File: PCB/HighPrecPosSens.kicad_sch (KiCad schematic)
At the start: 85 parts, among them J1 Conn_01x02_Male, J2 Conn_01x02_Male, J3 Conn_01x02_Male, J4 Conn_01x02_Male, J5 Conn_01x06_Male, U1 ST1S14PHR, U2 S12443, U3 LM393DR2G, U4 LM393DR2G, U5 74LVC541A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

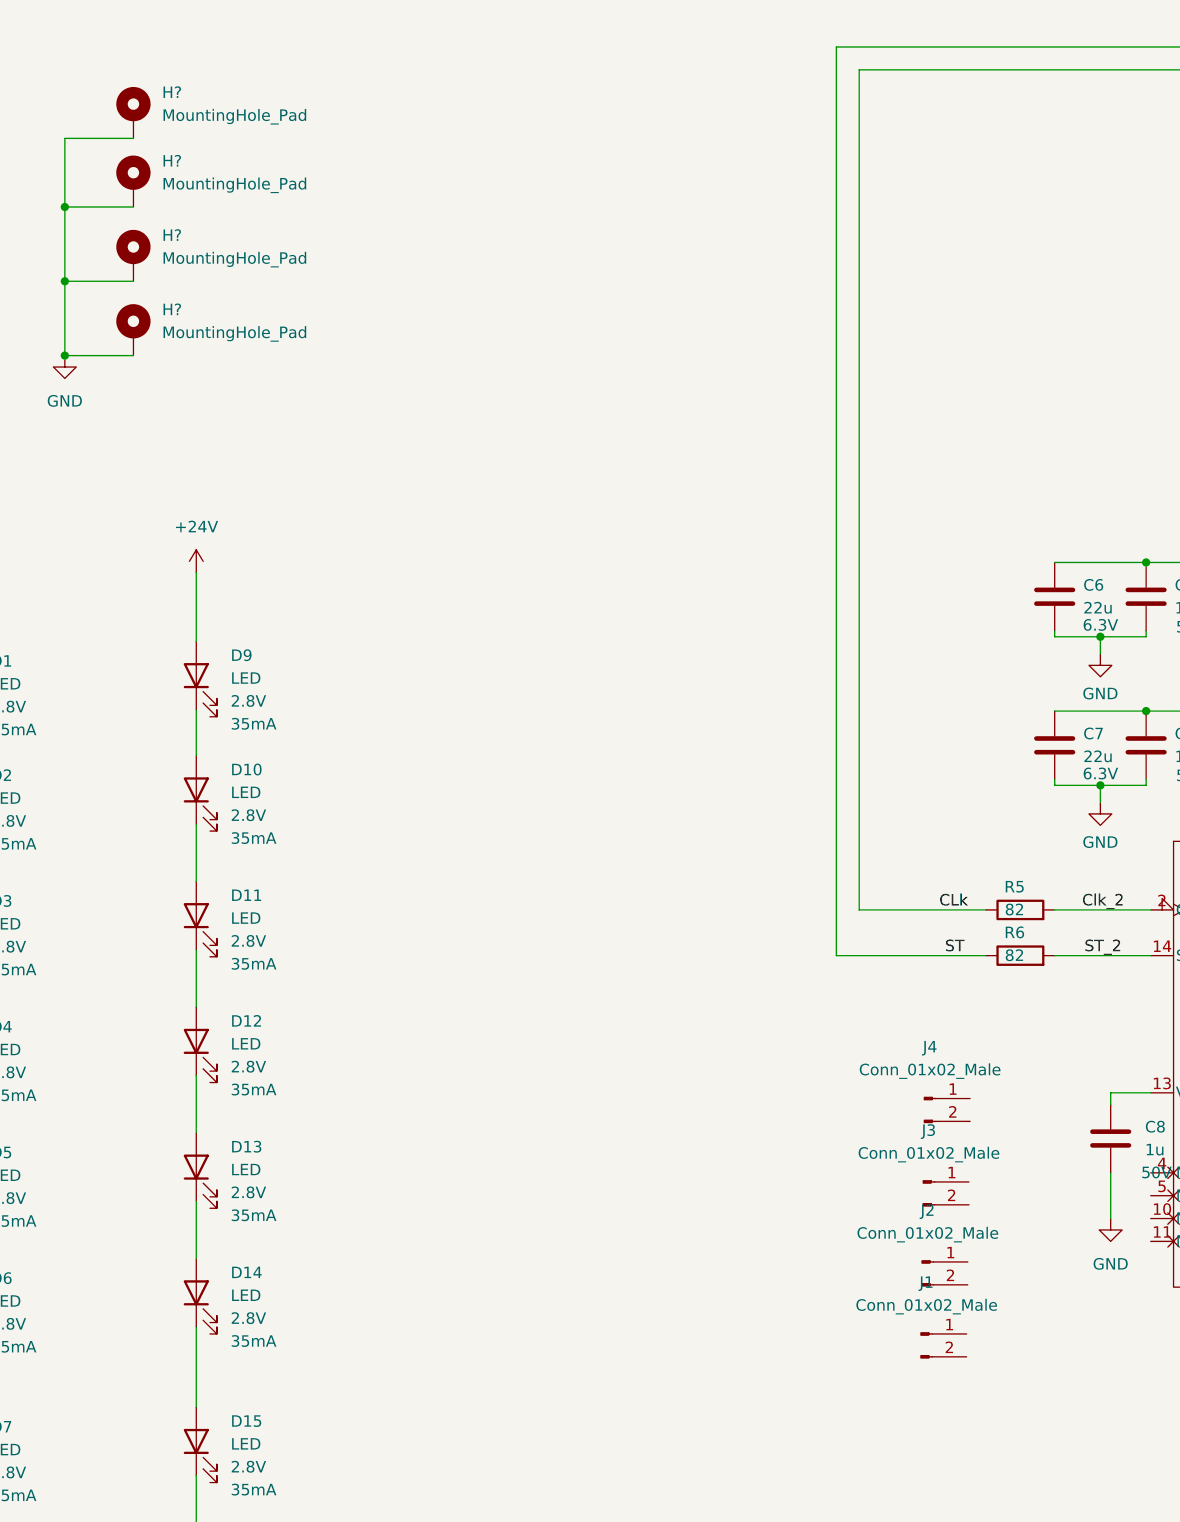
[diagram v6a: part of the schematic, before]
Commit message: Added some mounting or not definitions
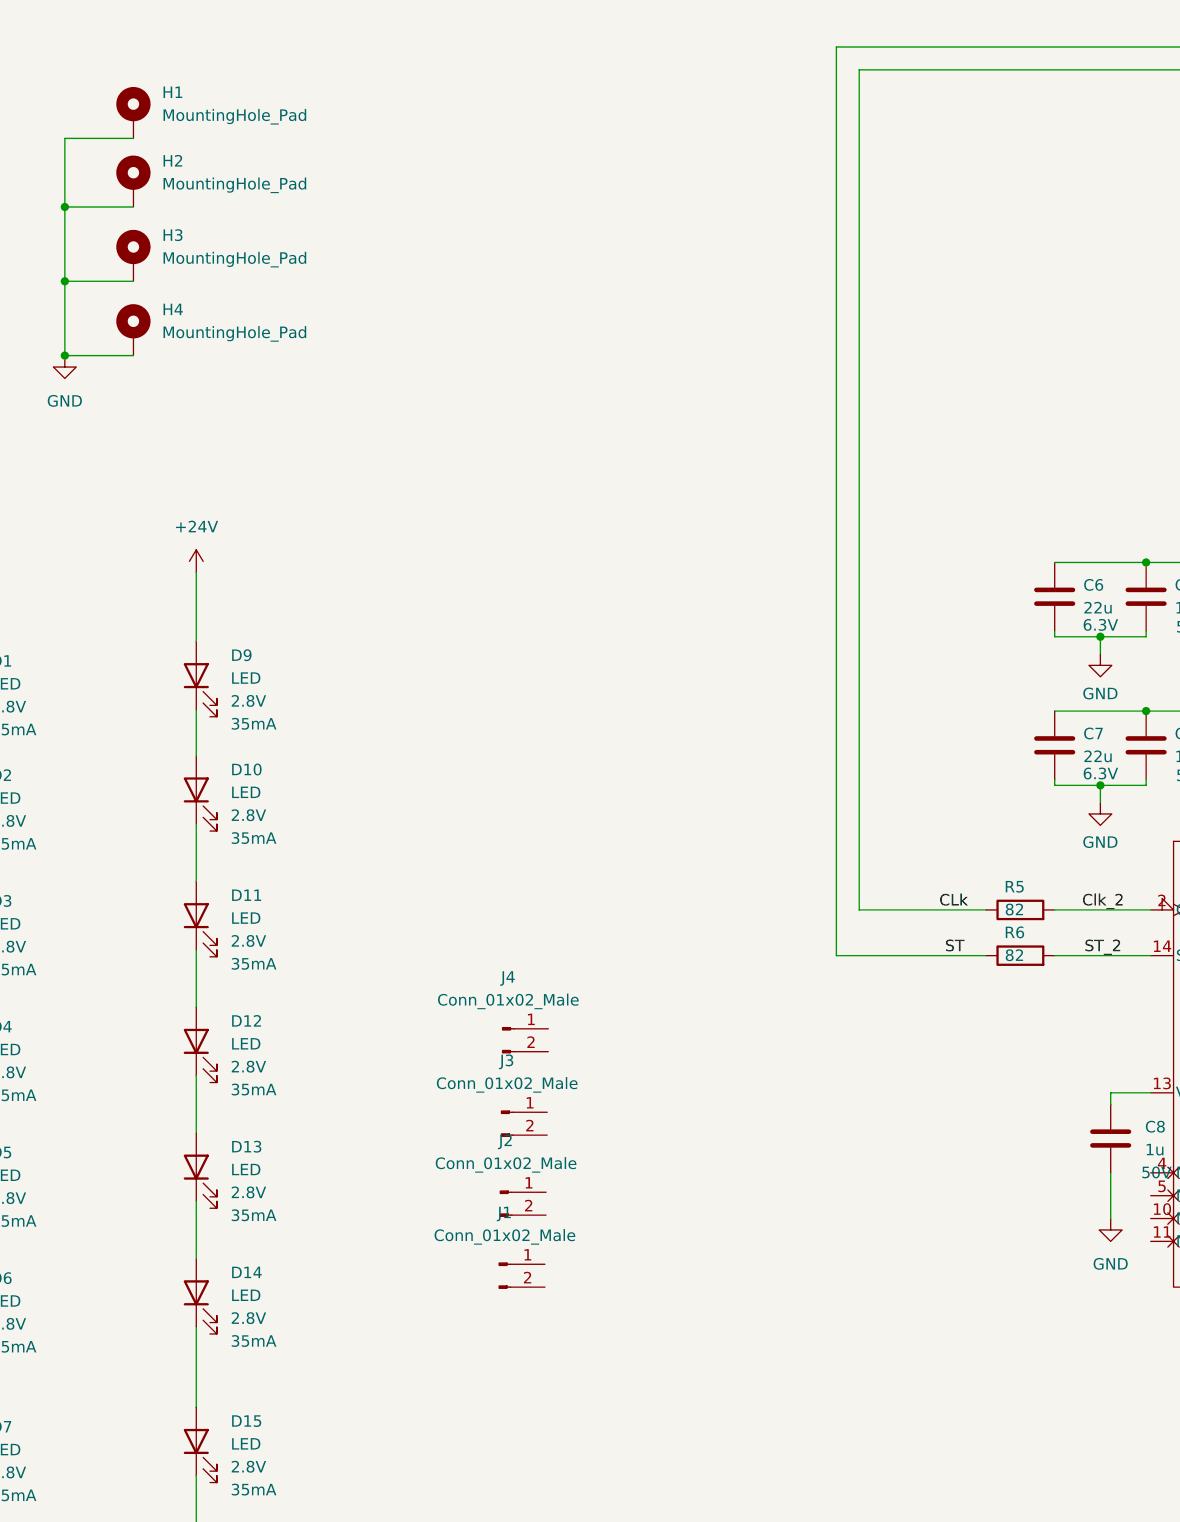
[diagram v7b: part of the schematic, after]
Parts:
- FID1, FID2, FID3, FID4, J1, J2, J3, J4, U2, U6: Mounting (none) -> DNP
- gave numbers to parts that had none: 4
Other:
- moved on the sheet: J1, J2, J3, J4
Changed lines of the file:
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@@
       (effects (font (size 1.27 1.27)) hide)
     )
+    (property "Mounting" "DNP" (id 4) (at 366.395 17.78 0)
+      (effects (font (size 1.27 1.27)) hide)
+    )
   )
   (symbol (lib_id "Device:LED") (at 71.12 127.635 90) (unit 1)
@@
   (symbol (lib_name "GND_3") (lib_id "power:GND") (at 56.515 51.435 0) (unit 1)
     (in_bom yes) (on_board yes) (fields_autoplaced)
-    (property "Reference" "#PWR?" (id 0) (at 56.515 57.785 0)
+    (property "Reference" "#PWR0105" (id 0) (at 56.515 57.785 0)
       (effects (font (size 1.27 1.27)) hide)
     )
@@
   (symbol (lib_id "Mechanical:MountingHole_Pad") (at 64.135 32.385 0) (unit 1)
     (in_bom yes) (on_board yes) (fields_autoplaced)
-    (property "Reference" "H?" (id 0) (at 67.31 29.8449 0)
+    (property "Reference" "H2" (id 0) (at 67.31 29.8449 0)
       (effects (font (size 1.27 1.27)) (justify left))
     )
@@
       (effects (font (size 1.27 1.27)) hide)
     )
+    (property "Mounting" "DNP" (id 5) (at 321.31 93.345 0)
+      (effects (font (size 1.27 1.27)) hide)
+    )
     (pin "1")
     (pin "10")
@@
       (effects (font (size 1.27 1.27)) hide)
     )
+    (property "Mounting" "DNP" (id 6) (at 189.865 100.33 0)
+      (effects (font (size 1.27 1.27)) hide)
+    )
     (pin "1")
     (pin "10")
@@
   (symbol (lib_id "Mechanical:MountingHole_Pad") (at 64.135 40.64 0) (unit 1)
     (in_bom yes) (on_board yes) (fields_autoplaced)
-    (property "Reference" "H?" (id 0) (at 67.31 38.0999 0)
+    (property "Reference" "H3" (id 0) (at 67.31 38.0999 0)
       (effects (font (size 1.27 1.27)) (justify left))
     )
@@
     (pin "2")
   )
-  (symbol (lib_id "Connector:Conn_01x02_Male") (at 151.638 160.147 0) (unit 1)
+  (symbol (lib_id "Connector:Conn_01x02_Male") (at 104.775 152.4 0) (unit 1)
     (in_bom yes) (on_board yes) (fields_autoplaced)
-    (property "Reference" "J1" (id 0) (at 152.273 154.432 0))
-    (property "Value" "Conn_01x02_Male" (id 1) (at 152.273 156.972 0))
-    (property "Footprint" "Connector_PinHeader_2.54mm:PinHeader_1x02_P2.54mm_Vertical" (id 2) (at 151.638 160.147 0)
+    (property "Reference" "J1" (id 0) (at 105.41 146.685 0))
+    (property "Value" "Conn_01x02_Male" (id 1) (at 105.41 149.225 0))
+    (property "Footprint" "Connector_PinHeader_2.54mm:PinHeader_1x02_P2.54mm_Vertical" (id 2) (at 104.775 152.4 0)
       (effects (font (size 1.27 1.27)) hide)
     )
-    (property "Datasheet" "~" (id 3) (at 151.638 160.147 0)
+    (property "Datasheet" "~" (id 3) (at 104.775 152.4 0)
+      (effects (font (size 1.27 1.27)) hide)
+    )
+    (property "Mounting" "DNP" (id 4) (at 104.775 152.4 0)
       (effects (font (size 1.27 1.27)) hide)
     )
@@
       (effects (font (size 1.27 1.27)) hide)
     )
+    (property "Mounting" "DNP" (id 4) (at 345.44 22.86 0)
+      (effects (font (size 1.27 1.27)) hide)
+    )
   )
   (symbol (lib_id "Device:R") (at 220.345 89.535 90) (unit 1)
@@
     (pin "8")
   )
-  (symbol (lib_id "Connector:Conn_01x02_Male") (at 152.019 133.985 0) (unit 1)
+  (symbol (lib_id "Connector:Conn_01x02_Male") (at 105.156 126.238 0) (unit 1)
     (in_bom yes) (on_board yes) (fields_autoplaced)
-    (property "Reference" "J4" (id 0) (at 152.654 128.27 0))
-    (property "Value" "Conn_01x02_Male" (id 1) (at 152.654 130.81 0))
-    (property "Footprint" "Connector_PinHeader_2.54mm:PinHeader_1x02_P2.54mm_Vertical" (id 2) (at 152.019 133.985 0)
+    (property "Reference" "J4" (id 0) (at 105.791 120.523 0))
+    (property "Value" "Conn_01x02_Male" (id 1) (at 105.791 123.063 0))
+    (property "Footprint" "Connector_PinHeader_2.54mm:PinHeader_1x02_P2.54mm_Vertical" (id 2) (at 105.156 126.238 0)
+      (effects (font (size 1.27 1.27)) hide)
+    )
+    (property "Datasheet" "~" (id 3) (at 105.156 126.238 0)
       (effects (font (size 1.27 1.27)) hide)
     )
-    (property "Datasheet" "~" (id 3) (at 152.019 133.985 0)
+    (property "Mounting" "DNP" (id 4) (at 105.156 126.238 0)
       (effects (font (size 1.27 1.27)) hide)
     )
@@
       (effects (font (size 1.27 1.27)) hide)
     )
+    (property "Mounting" "DNP" (id 4) (at 345.44 16.51 0)
+      (effects (font (size 1.27 1.27)) hide)
+    )
   )
   (symbol (lib_id "Device:R") (at 372.11 172.72 90) (unit 1)
@@
     (pin "2")
   )
-  (symbol (lib_id "Connector:Conn_01x02_Male") (at 151.765 152.146 0) (unit 1)
+  (symbol (lib_id "Connector:Conn_01x02_Male") (at 104.902 144.399 0) (unit 1)
     (in_bom yes) (on_board yes) (fields_autoplaced)
-    (property "Reference" "J2" (id 0) (at 152.4 146.431 0))
-    (property "Value" "Conn_01x02_Male" (id 1) (at 152.4 148.971 0))
-    (property "Footprint" "Connector_PinHeader_2.54mm:PinHeader_1x02_P2.54mm_Vertical" (id 2) (at 151.765 152.146 0)
+    (property "Reference" "J2" (id 0) (at 105.537 138.684 0))
+    (property "Value" "Conn_01x02_Male" (id 1) (at 105.537 141.224 0))
+    (property "Footprint" "Connector_PinHeader_2.54mm:PinHeader_1x02_P2.54mm_Vertical" (id 2) (at 104.902 144.399 0)
+      (effects (font (size 1.27 1.27)) hide)
+    )
+    (property "Datasheet" "~" (id 3) (at 104.902 144.399 0)
       (effects (font (size 1.27 1.27)) hide)
     )
-    (property "Datasheet" "~" (id 3) (at 151.765 152.146 0)
+    (property "Mounting" "DNP" (id 4) (at 104.902 144.399 0)
       (effects (font (size 1.27 1.27)) hide)
     )
@@
   (symbol (lib_id "Mechanical:MountingHole_Pad") (at 64.135 48.895 0) (unit 1)
     (in_bom yes) (on_board yes) (fields_autoplaced)
-    (property "Reference" "H?" (id 0) (at 67.31 46.3549 0)
+    (property "Reference" "H4" (id 0) (at 67.31 46.3549 0)
       (effects (font (size 1.27 1.27)) (justify left))
     )
@@
       (effects (font (size 1.27 1.27)) hide)
     )
+    (property "Mounting" "DNP" (id 4) (at 366.395 24.13 0)
+      (effects (font (size 1.27 1.27)) hide)
+    )
   )
   (symbol (lib_id "power:+3.3V") (at 106.68 247.65 0) (unit 1)
@@
     (pin "2")
   )
-  (symbol (lib_id "Connector:Conn_01x02_Male") (at 151.892 143.256 0) (unit 1)
+  (symbol (lib_id "Connector:Conn_01x02_Male") (at 105.029 135.509 0) (unit 1)
     (in_bom yes) (on_board yes) (fields_autoplaced)
-    (property "Reference" "J3" (id 0) (at 152.527 137.541 0))
-    (property "Value" "Conn_01x02_Male" (id 1) (at 152.527 140.081 0))
-    (property "Footprint" "Connector_PinHeader_2.54mm:PinHeader_1x02_P2.54mm_Vertical" (id 2) (at 151.892 143.256 0)
+    (property "Reference" "J3" (id 0) (at 105.664 129.794 0))
+    (property "Value" "Conn_01x02_Male" (id 1) (at 105.664 132.334 0))
+    (property "Footprint" "Connector_PinHeader_2.54mm:PinHeader_1x02_P2.54mm_Vertical" (id 2) (at 105.029 135.509 0)
       (effects (font (size 1.27 1.27)) hide)
     )
-    (property "Datasheet" "~" (id 3) (at 151.892 143.256 0)
+    (property "Datasheet" "~" (id 3) (at 105.029 135.509 0)
+      (effects (font (size 1.27 1.27)) hide)
+    )
+    (property "Mounting" "DNP" (id 4) (at 105.029 135.509 0)
       (effects (font (size 1.27 1.27)) hide)
     )
@@
   (symbol (lib_id "Mechanical:MountingHole_Pad") (at 64.135 24.765 0) (unit 1)
     (in_bom yes) (on_board yes) (fields_autoplaced)
-    (property "Reference" "H?" (id 0) (at 67.31 22.2249 0)
+    (property "Reference" "H1" (id 0) (at 67.31 22.2249 0)
       (effects (font (size 1.27 1.27)) (justify left))
     )
@@
     )
     (path "/0dd7dee9-a19e-40f5-92fc-3bb6245e2c70"
-      (reference "#PWR?") (unit 1) (value "GND") (footprint "")
+      (reference "#PWR0105") (unit 1) (value "GND") (footprint "")
     )
     (path "/6f052ed9-6923-4aad-9ce7-77a831335223"
@@
       (reference "FID4") (unit 1) (value "Fiducial") (footprint "Fiducial:Fiducial_1mm_Mask2mm")
     )
+    (path "/cffb5fac-e82d-404f-bf3f-17054244c031"
+      (reference "H1") (unit 1) (value "MountingHole_Pad") (footprint "MountingHole:MountingHole_3.2mm_M3_Pad")
+    )
     (path "/2e4d5ac6-38f9-4500-bf48-9501c64ee03e"
-      (reference "H?") (unit 1) (value "MountingHole_Pad") (footprint "MountingHole:MountingHole_3.2mm_M3_Pad")
+      (reference "H2") (unit 1) (value "MountingHole_Pad") (footprint "MountingHole:MountingHole_3.2mm_M3_Pad")
     )
     (path "/82df9250-4165-47dc-b1f7-05adb7a466ed"
-      (reference "H?") (unit 1) (value "MountingHole_Pad") (footprint "MountingHole:MountingHole_3.2mm_M3_Pad")
+      (reference "H3") (unit 1) (value "MountingHole_Pad") (footprint "MountingHole:MountingHole_3.2mm_M3_Pad")
     )
     (path "/b196d5b8-e474-4682-9489-9dbbd3f0927b"
-      (reference "H?") (unit 1) (value "MountingHole_Pad") (footprint "MountingHole:MountingHole_3.2mm_M3_Pad")
-    )
-    (path "/cffb5fac-e82d-404f-bf3f-17054244c031"
-      (reference "H?") (unit 1) (value "MountingHole_Pad") (footprint "MountingHole:MountingHole_3.2mm_M3_Pad")
+      (reference "H4") (unit 1) (value "MountingHole_Pad") (footprint "MountingHole:MountingHole_3.2mm_M3_Pad")
     )
     (path "/8d7aa37b-4484-4215-9461-6291d9f92a28"
